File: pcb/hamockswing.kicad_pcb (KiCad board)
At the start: 2 copper layers, 49.5 x 23.5 mm, 12 parts, among them J1 Conn_01x06, J2 Conn_01x06, J3 Conn_01x03, Q1 Q_NMOS_GDS, U1 ATmega88-20A

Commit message: stuff
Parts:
- added C1: C, Capacitor_SMD:C_0603_1608Metric, F.Cu at (86.4, 99.1)
- added C2: C, Capacitor_SMD:C_0603_1608Metric, F.Cu at (98.6, 100.1)
- added C4: C, Capacitor_SMD:C_0603_1608Metric, F.Cu at (98.6, 103.1)
- added C5: C, Capacitor_SMD:C_0603_1608Metric, F.Cu at (86.4, 102.4)
- added C6: C, Capacitor_SMD:C_0603_1608Metric, F.Cu at (97.8, 92.6)
- added H1: MountingHole, MountingHole:MountingHole_3.2mm_M3_ISO7380_Pad, F.Cu at (82.5, 92.2)
- added H2: MountingHole, MountingHole:MountingHole_3.2mm_M3_ISO7380_Pad, F.Cu at (82.8, 108.7)
- moved J2 2.99 mm to (81.3, 98.1)
- moved U1 1.52 mm to (92.5, 103.2)
- moved C3 0.13 mm to (94.9, 109.9)
- moved R3 0.13 mm to (91.8, 109.9)
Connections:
- D1 pad 1: +5V -> MOTOR+
- D1 pad 2: Net-(D1-Pad2) -> +5V
- D2 pad 1: MOTOR -> +5V
- D2 pad 2: Net-(D1-Pad2) -> MOTOR-
- J1 pad 1: MOTOR -> MOTOR+
- J1 pad 2: GND -> MOTOR-
- Q1 pad 2: Net-(D1-Pad2) -> MOTOR-
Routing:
- net MOTOR-: track 0.00 -> 8.99 mm
- net Net-(D1-Pad2): track 7.08 -> 0.00 mm
- net +5V: track 48.7 -> 55.6 mm
- net GND: track 16.8 -> 21.7 mm, vias 7 -> 10
- net RST: track 22.1 -> 25.9 mm
- net MOTOR: track 2.92 -> 0.00 mm
- net SCK: track 9.93 -> 8.07 mm
- net MISO: track 8.68 -> 10.4 mm
- net ENC A: track 7.74 -> 9.38 mm
- net TX: track 6.67 -> 7.95 mm
- net MOSI: track 18.9 -> 19.8 mm
- net ENC B: track 10.5 -> 9.67 mm
- net LED: track 2.17 -> 2.98 mm
- added copper zone on F.Cu, net GND
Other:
- board size 49.5 x 23.5 mm -> 33.3 x 24.4 mm
- board text added: "+5V"
- board text added: "ENC +"
- board text added: "ENC -"
- board text added: "ENC A"
- board text added: "ENC B"
- board text added: "GND"
- board text added: "M+"
- board text added: "M-"
- board text added: "TX"

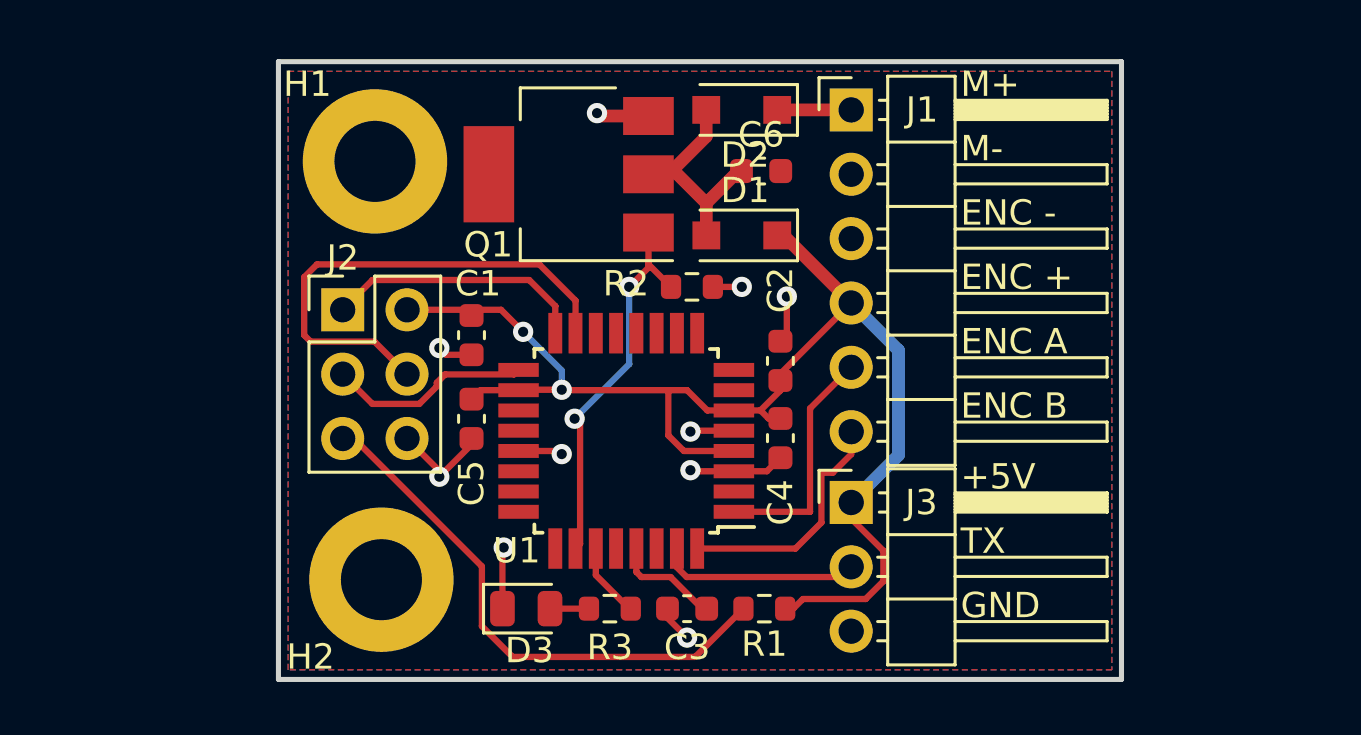
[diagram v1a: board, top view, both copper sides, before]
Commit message: kind of works, pcb as delivered to eurocircuits
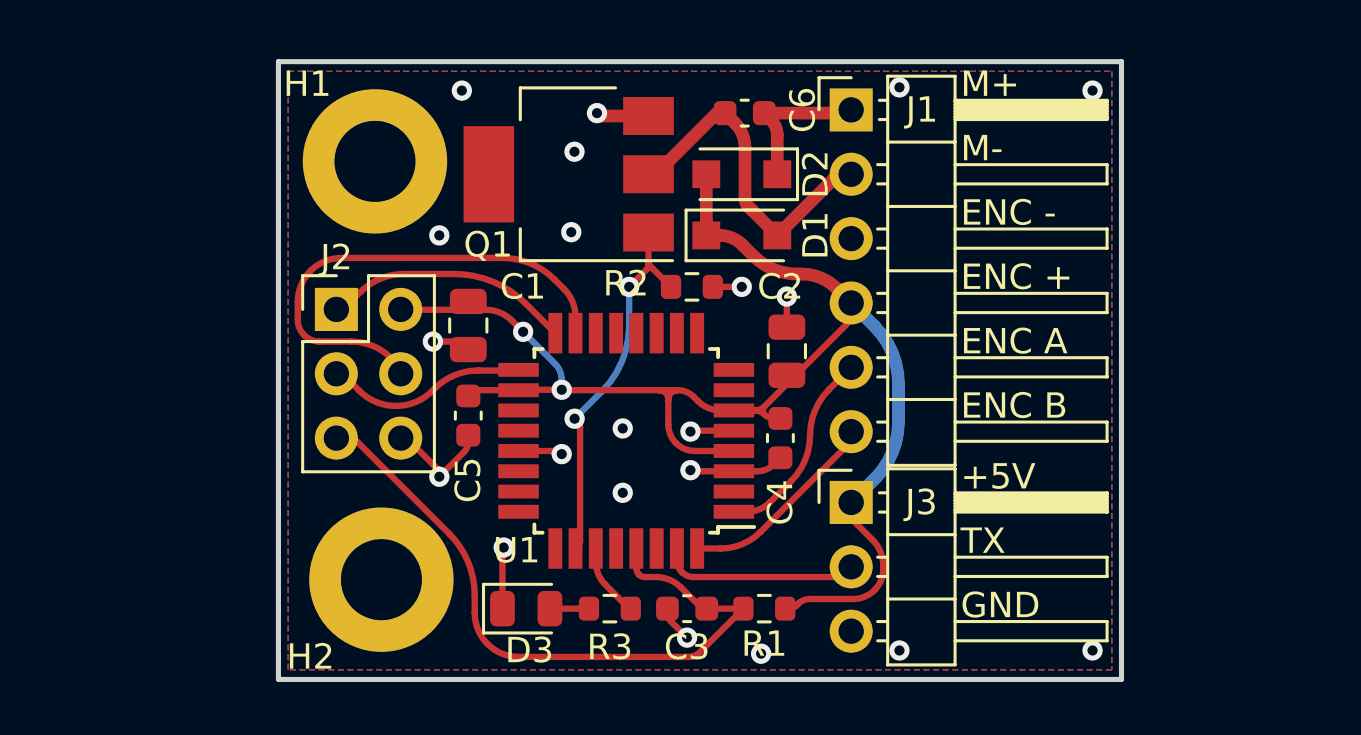
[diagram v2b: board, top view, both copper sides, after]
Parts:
- C1, C2: footprint Capacitor_SMD:C_0603_1608Metric -> Capacitor_SMD:C_0805_2012Metric
- moved D2 4.95 mm to (97.0, 95.1), turned to 0 degrees
- moved D1 2.41 mm to (97.0, 92.7)
- moved C6 2.38 mm to (97.1, 90.3)
- moved C2 0.46 mm to (98.8, 99.7)
- moved C1 0.40 mm to (86.2, 98.7)
- moved J2 0.25 mm to (81.0, 98.0)
- moved C5 0.18 mm to (86.2, 102.2)
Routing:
- net MOTOR+: track 0.00 -> 6.05 mm
- net MOTOR-: track 8.99 -> 13.2 mm
- net +5V: track 55.6 -> 57.5 mm
- net ENC B: track 9.67 -> 8.08 mm
- net ENC A: track 9.38 -> 7.93 mm
- net RST: track 25.9 -> 27.1 mm
- net MISO: track 10.4 -> 9.64 mm
- net GND: track 21.7 -> 21.5 mm, vias 10 -> 21

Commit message: new
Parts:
- removed H1, H2: MountingHole, MountingHole:MountingHole_3.2mm_M3_ISO7380_Pad
- C1, C2: footprint Capacitor_SMD:C_0805_2012Metric -> Capacitor_SMD:C_0603_1608Metric
- C4, C5: footprint Capacitor_SMD:C_0603_1608Metric -> Capacitor_SMD:C_0805_2012Metric
- moved C5 13.2 mm to (98.8, 98.4)
- moved C4 13.0 mm to (86.4, 98.7)
- moved C1 12.9 mm to (98.7, 102.0)
- moved C2 12.9 mm to (86.2, 102.5), turned to 90 degrees
- moved D1 2.80 mm to (97.2, 92.3)
- moved D2 2.16 mm to (97.2, 94.9), turned to 0 degrees
- renumbered D2 to D1, D1 to D2
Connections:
- D1 pad 2: MOTOR- -> MOTOR+
- D2 pad 1: MOTOR+ -> +5V
- D2 pad 2: +5V -> MOTOR-
- U1 pad 13: unconnected-(U1-Pad13) -> Net-(Q1-Pad1)
- U1 pad 26: Net-(Q1-Pad1) -> unconnected-(U1-Pad26)
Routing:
- net Net-(Q1-Pad1): track 15.0 -> 5.87 mm, vias 2 -> 0
- net GND: track 21.5 -> 22.9 mm
